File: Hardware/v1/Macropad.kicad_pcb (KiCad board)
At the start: 2 copper layers, 89 x 130.9 mm, 172 parts, among them J1 USB_C_Receptacle_USB2.0, J2 Conn_01x04_Female, J3 Conn_02x03_Odd_Even, J4 USB_C_Receptacle_USB2.0, J5 USB_C_Receptacle_USB2.0, J6 USB_C_Receptacle_USB2.0, SW1 K40_1U, SW10 K01_1U, SW11 K42_1U, SW12 K32_1U, SW13 K22_1U, SW14 K12_1U, SW15 K02_1U, SW16 K43_1U, SW17 K33_1U, SW18 K23_1U, SW19 K13_1U, SW2 K30_1U, SW20 K03_1U, SW21 Rotary_Encoder_Switch, SW22 SW_Push, SW3 K20_1U, SW4 K10_1U, SW5 K00_1U, SW6 K41_1U, SW7 K31_1U, SW8 K21_1U, SW9 K11_1U, U1 TCR2EF33, U2 SRV05-4, U4 TUSB2046b, U5 ATmega32U4-AU, U6 SRV05-4, U8 SRV05-4, X1 KC2016K, X2 625L3C006M00000

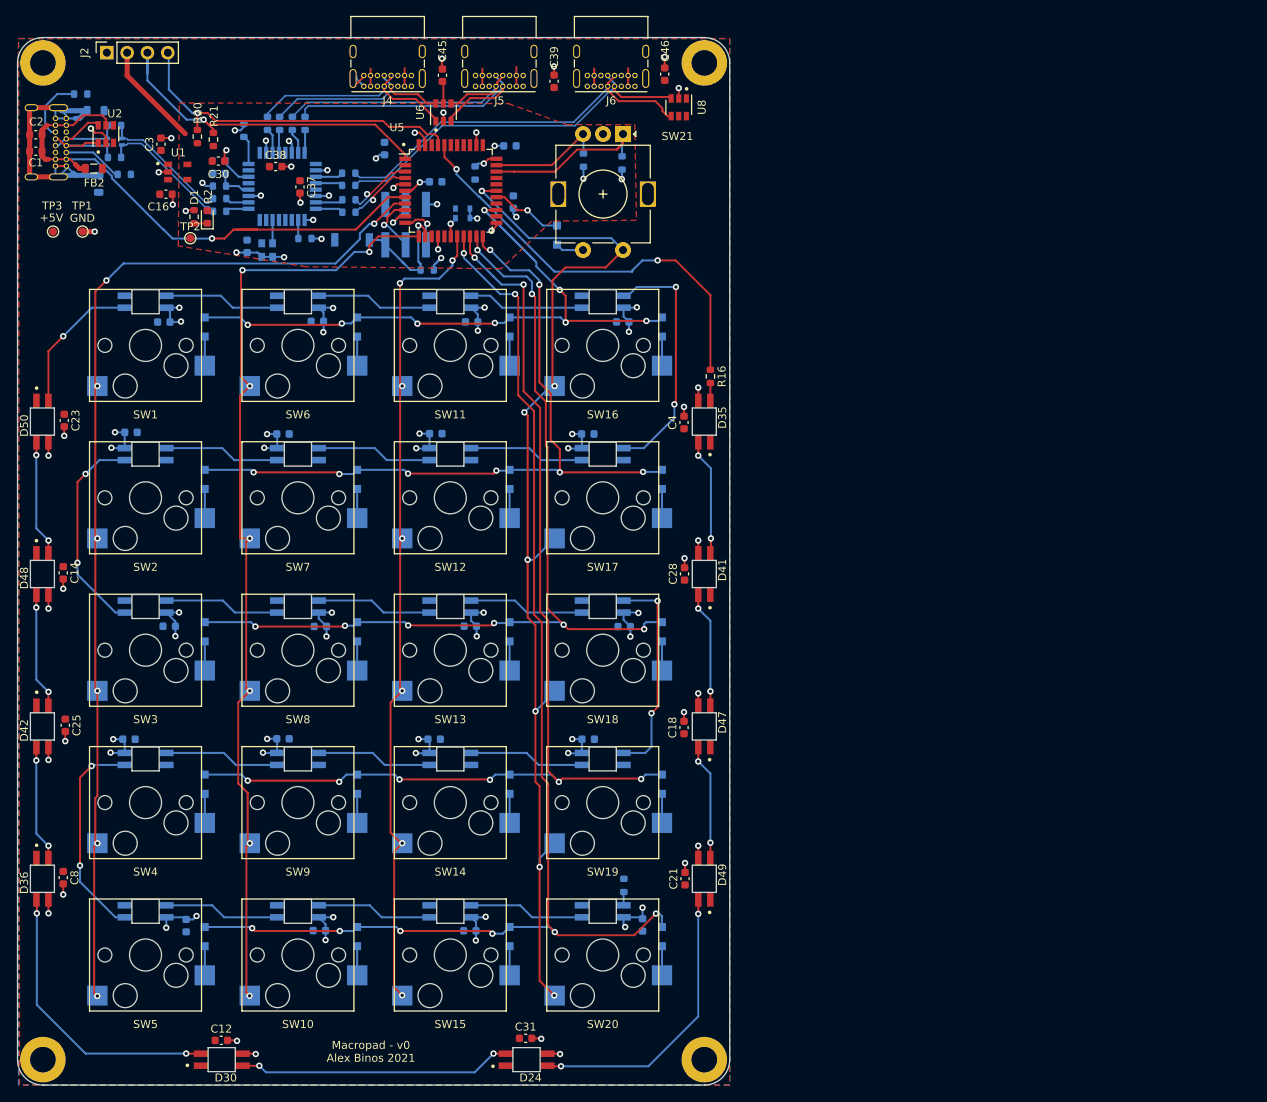
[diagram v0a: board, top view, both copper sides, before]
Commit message: Moving underglow LED and USB VBUS decoupling caps
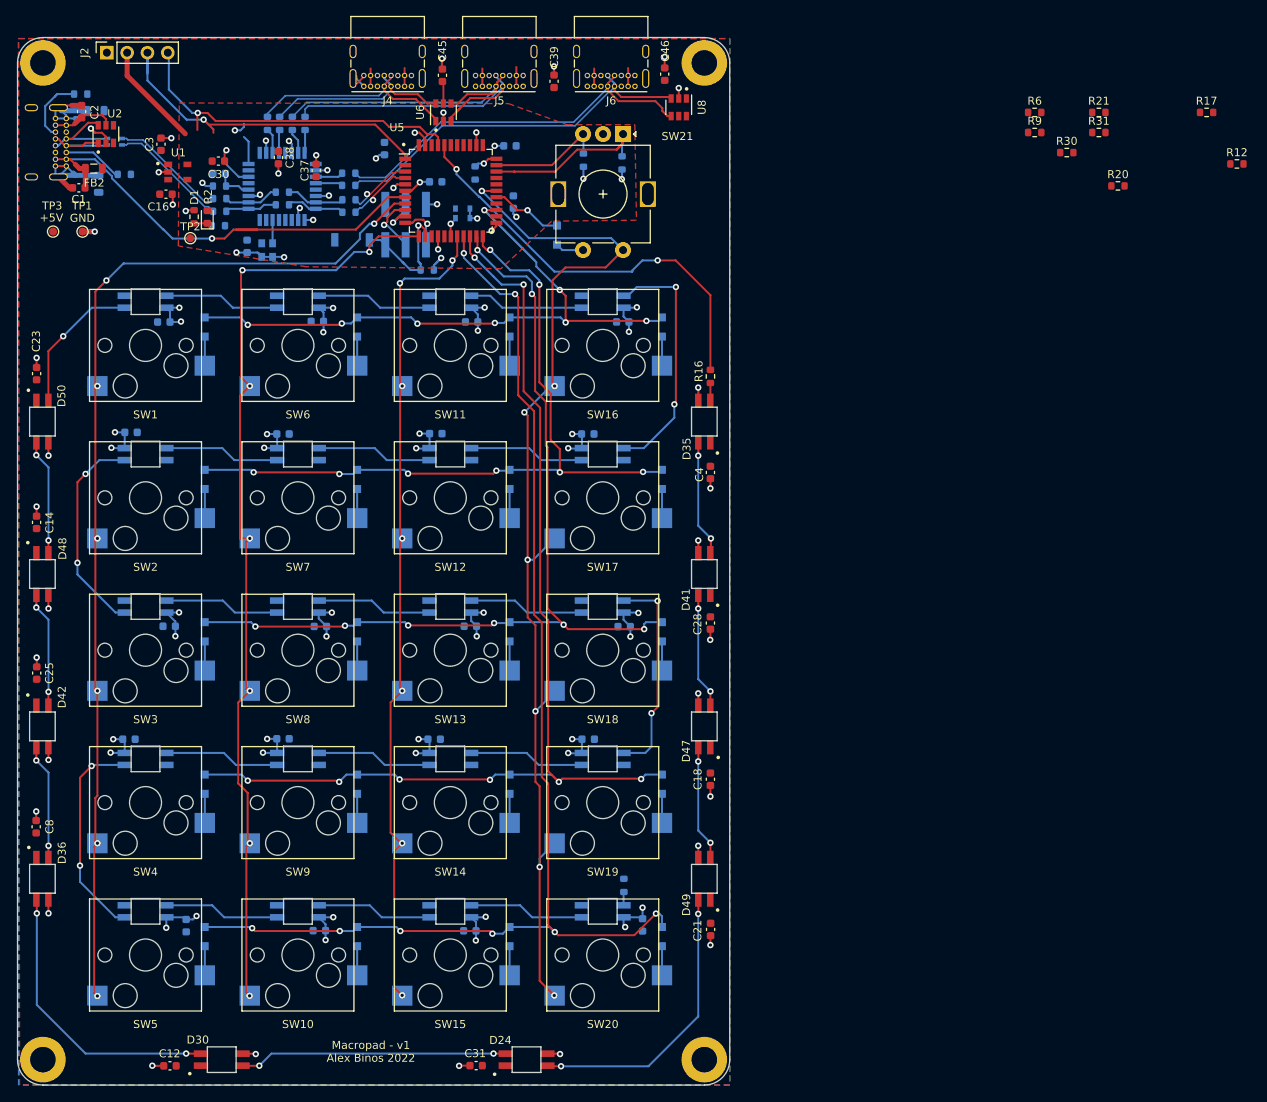
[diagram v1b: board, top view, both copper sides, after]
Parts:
- added R12: 4K7, resistor_smd:R_0603_1608Metric, F.Cu at (196.1, 75.4)
- added R17: 4K7, resistor_smd:R_0603_1608Metric, F.Cu at (192.3, 68.9)
- added R30: 15K, resistor_smd:R_0603_1608Metric, F.Cu at (174.8, 73.9)
- added R31: 15K, resistor_smd:R_0603_1608Metric, F.Cu at (178.9, 71.4)
- R10, R11: value 4K7 -> OPT
- R20, R21: value 4K7 -> 15K
- R5: value OPT -> 1K5
- R6: value OPT -> 15K; moved to F.Cu
- R9: value 4K7 -> 15K; moved to F.Cu
- moved R20 115.2 mm to (181.2, 78.1), turned to 0 degrees
- moved R6 115.2 mm to (170.8, 68.9), turned to 0 degrees
- moved R21 110.7 mm to (178.9, 68.9), turned to 0 degrees
- moved R9 92.2 mm to (170.8, 71.4)
- moved R5 18.0 mm to (68.8, 83.1), turned to 0 degrees
- moved R10 9.64 mm to (76.8, 80.5), turned to 180 degrees
- moved R11 9.11 mm to (76.8, 78.9), turned to 180 degrees
- moved C25 7.44 mm to (46.1, 139.0), turned to 90 degrees
- moved C18 7.26 mm to (130.3, 152.3), turned to 270 degrees
- moved C8 7.21 mm to (46.0, 158.2), turned to 90 degrees
- moved C12 7.17 mm to (62.7, 188.1), turned to 180 degrees
- moved C14 7.14 mm to (46.1, 120.2), turned to 90 degrees
- moved C21 7.10 mm to (130.3, 171.1), turned to 270 degrees
- moved C4 7.07 mm to (130.3, 113.9), turned to 270 degrees
- moved C31 7.06 mm to (101.0, 188.1), turned to 180 degrees
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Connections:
- R10 pad 1: GND -> /USB_HUB/D4+
- R10 pad 2: Net-(R10-Pad2) -> USB_D0+
- R11 pad 1: Net-(R11-Pad1) -> /USB_HUB/D4-
- R11 pad 2: +3V3 -> USB_D0-
- R20 pad 1: +3V3 -> USB_D2+
- R20 pad 2: SDA -> GND
- R21 pad 1: +3V3 -> USB_D3+
- R21 pad 2: SCL -> GND
- R5 pad 1: /USB/D- -> +3V3
- R5 pad 2: Net-(J1-PadA7) -> USB_D0+
- R6 pad 1: /USB/D+ -> USB_D1+
- R6 pad 2: Net-(J1-PadA6) -> GND
- R9 pad 1: Net-(R9-Pad1) -> USB_D1-
- R9 pad 2: +3V3 -> GND
- U4 pad 26: Net-(R9-Pad1) -> +3V3
- U4 pad 6: Net-(R10-Pad2) -> GND
- U4 pad 8: Net-(R11-Pad1) -> GND
- U5 pad 1: SCL -> COL[2]
- U5 pad 18: COL[2] -> SCL
- U5 pad 19: ROW[0] -> SDA
- U5 pad 41: SDA -> ROW[0]
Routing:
- net Net-(C1-Pad2): track 38.3 -> 28.4 mm
- net GND: track 59.7 -> 68.8 mm
- net USB_D0-: track 2.98 -> 6.91 mm
- net Net-(R10-Pad2): track 3.90 -> 0.00 mm
- net /USB_HUB/D4-: track 3.46 -> 7.34 mm
- net /USB_HUB/D4+: track 3.50 -> 7.32 mm
- net Net-(R11-Pad1): track 3.63 -> 0.00 mm
- net USB_D0+: track 2.92 -> 6.52 mm
- net VBUS: track 70.4 -> 67.1 mm
- net Net-(R9-Pad1): track 2.32 -> 0.00 mm
- net /USB/D-: track 16.7 -> 15.0 mm
- net Net-(J1-PadA7): track 13.5 -> 11.8 mm
- net /USB/D+: track 16.6 -> 15.0 mm
- net Net-(J1-PadA6): track 12.8 -> 11.1 mm
- net Net-(D24-Pad2): track 34.2 -> 33.5 mm
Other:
- board text added: "Macropad - v1 Alex Binos 2022"
- board text removed: "Macropad - v0 Alex Binos 2021"

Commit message: Connected USB resistors
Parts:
- C34, R19: moved to F.Cu
- R20, R21, R30, R31, R6, R9: moved to B.Cu
- moved R12 136.6 mm to (59.9, 65.2), turned to 90 degrees
- moved R17 129.9 mm to (62.5, 65.2), turned to 90 degrees
- moved R9 99.3 mm to (71.5, 68.7), turned to 90 degrees
- moved R20 98.0 mm to (83.5, 71.1), turned to 270 degrees
- moved R6 97.6 mm to (73.2, 69.4), turned to 90 degrees
- moved R21 94.6 mm to (84.4, 73.4), turned to 180 degrees
- moved R31 93.8 mm to (85.1, 74.9), turned to 180 degrees
- moved R30 93.2 mm to (81.7, 70.1), turned to 90 degrees
- moved R19 6.25 mm to (106.7, 74.1), turned to 0 degrees
- moved TP2 5.13 mm to (65.7, 79.5)
- moved R18 4.54 mm to (90.4, 88.5), turned to 0 degrees
- moved C36 4.08 mm to (93.6, 73.0), turned to 0 degrees
- moved D1 3.85 mm to (63.6, 82.4), turned to 0 degrees
- moved C30 3.01 mm to (66.2, 73.6)
- moved R2 2.99 mm to (63.6, 84.0), turned to 180 degrees
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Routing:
- net SCL: track 44.8 -> 63.3 mm, vias 1 -> 3
- net ROW[0]: track 154.1 -> 170.1 mm
- net SDA: track 43.9 -> 59.8 mm, vias 1 -> 3
- net COL[2]: track 103.2 -> 115.0 mm
- net USB_D3+: track 48.6 -> 55.8 mm
- net +3V3: track 46.5 -> 53.0 mm, vias 19 -> 18
- net USB_D2-: track 35.9 -> 40.2 mm
- net USB_D2+: track 38.0 -> 42.2 mm
- net USB_D1+: track 24.3 -> 27.8 mm
- net USB_D1-: track 27.4 -> 30.8 mm
- net GND: track 68.8 -> 65.6 mm, vias 39 -> 41
- net Net-(C33-Pad1): track 3.50 -> 6.30 mm
- net USB_D3-: track 48.5 -> 51.0 mm
- net USB_D0+: track 6.52 -> 8.80 mm
- net RST: track 16.2 -> 14.5 mm
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
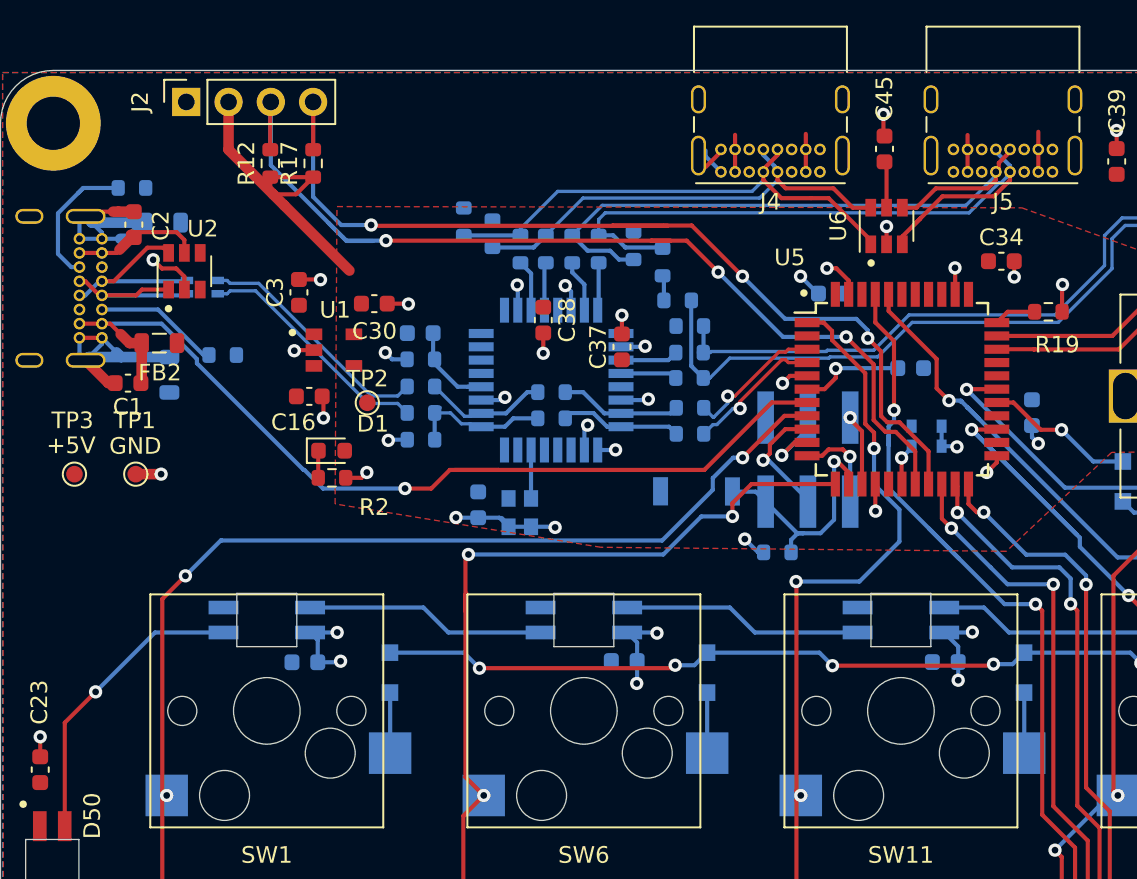
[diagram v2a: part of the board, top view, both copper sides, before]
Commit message: Disconecting mounting holes from ground Adding schmitt trigger bugger to USB HUB reset Cleaning up routing and fixing plane connections
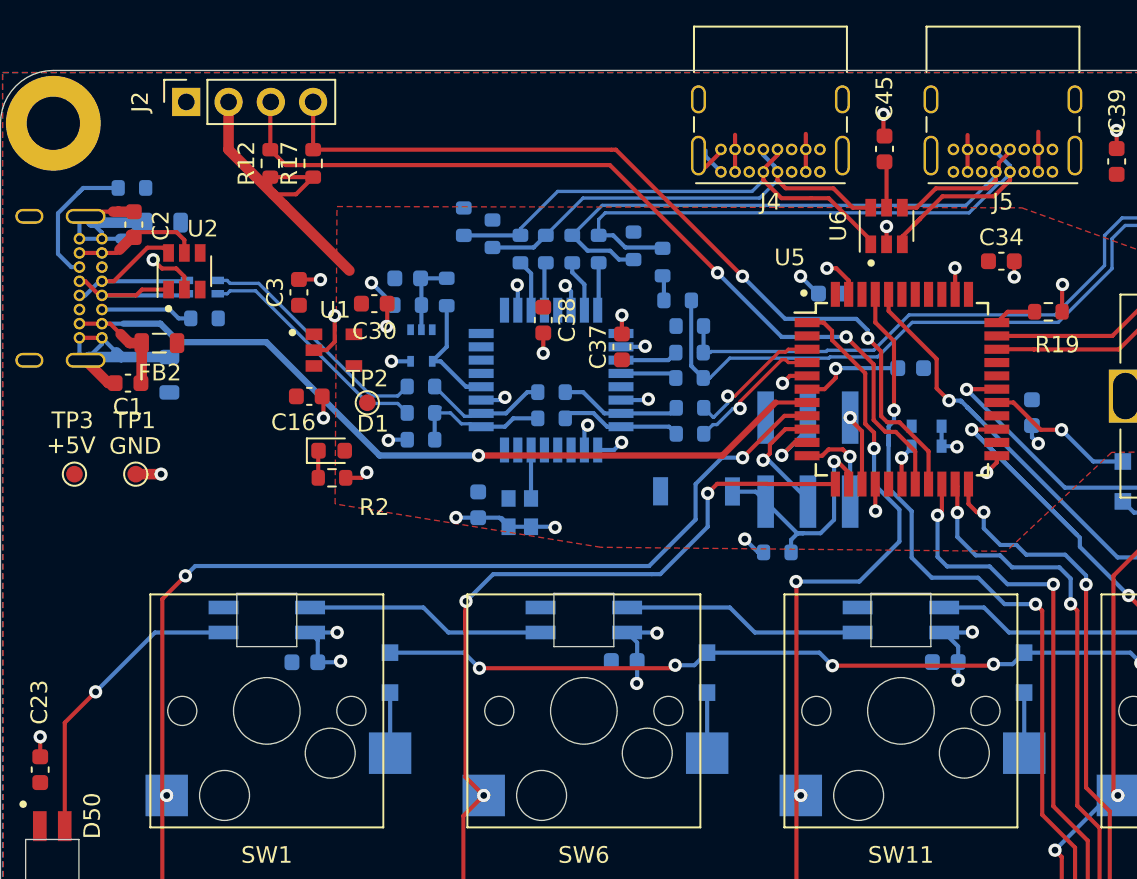
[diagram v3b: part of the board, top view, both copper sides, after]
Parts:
- added R32: OPT, resistor_smd:R_0603_1608Metric, B.Cu at (70.5, 72.9)
- added U3: 74AHC1G17, Package_TO_SOT_SMD:SOT-353_SC-70-5, B.Cu at (69.0, 76.1)
- moved C44 3.38 mm to (68.2, 72.1)
- moved R1 3.35 mm to (68.2, 73.7)
- moved R4 2.46 mm to (55.9, 74.5)
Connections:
- H1 pad 1: GND -> Net-(H1-Pad1)
- H2 pad 1: GND -> Net-(H2-Pad1)
- H3 pad 1: GND -> Net-(H3-Pad1)
- H4 pad 1: GND -> Net-(H4-Pad1)
- U4 pad 4: Net-(C44-Pad2) -> Net-(R32-Pad2)
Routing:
- net SCL: track 63.3 -> 53.1 mm, vias 3 -> 2
- net Net-(R32-Pad2): track 0.00 -> 8.09 mm
- net SDA: track 59.8 -> 51.9 mm, vias 3 -> 2
- net VBUS: track 67.1 -> 62.6 mm
- net +3V3: track 53.0 -> 55.1 mm, vias 18 -> 19
- net Net-(J1-PadA5): track 7.56 -> 5.56 mm
- net GND: track 65.6 -> 67.5 mm
- net ROW[1]: track 133.6 -> 135.4 mm
- net Net-(C44-Pad2): track 6.06 -> 4.68 mm
- net ROW[0]: track 170.1 -> 169.3 mm
- net ROW[2]: track 113.8 -> 114.6 mm
- net COL[0]: track 132.9 -> 133.8 mm
- net COL[1]: track 120.4 -> 119.6 mm
- net ROW[3]: track 93.3 -> 93.9 mm
